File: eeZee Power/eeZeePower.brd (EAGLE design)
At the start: 26 x 12.7 mm, 11 parts

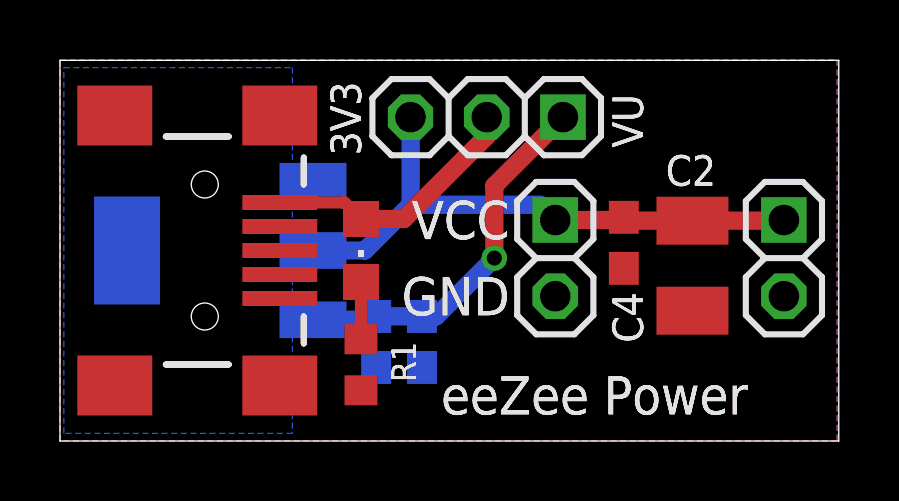
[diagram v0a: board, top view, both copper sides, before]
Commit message: Fixed jumper labels
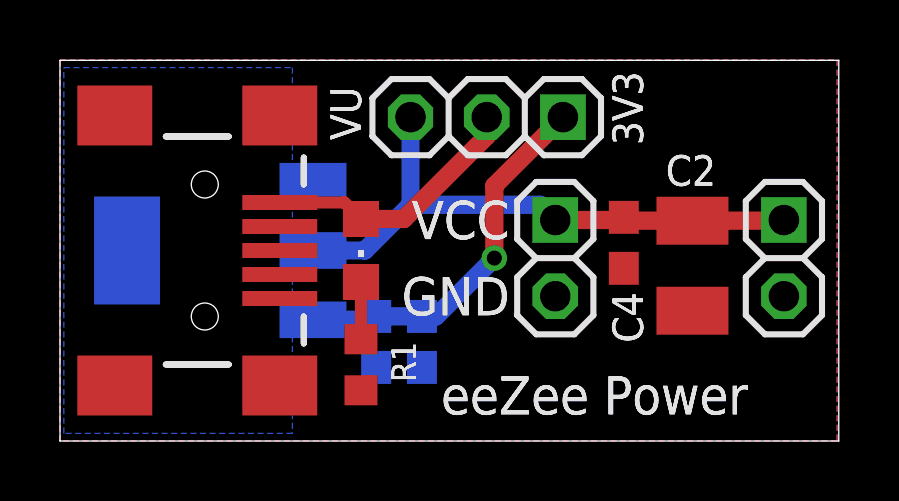
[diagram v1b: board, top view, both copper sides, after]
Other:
- board text added: "Rev 0.2"
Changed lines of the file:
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@@
 <layer number="19" name="Unrouted" color="6" fill="1" visible="yes" active="yes"/>
 <layer number="20" name="Dimension" color="15" fill="1" visible="yes" active="yes"/>
-<layer number="21" name="tPlace" color="7" fill="1" visible="no" active="yes"/>
+<layer number="21" name="tPlace" color="7" fill="1" visible="yes" active="yes"/>
 <layer number="22" name="bPlace" color="7" fill="1" visible="no" active="yes"/>
 <layer number="23" name="tOrigins" color="15" fill="1" visible="no" active="yes"/>
 <layer number="24" name="bOrigins" color="15" fill="1" visible="no" active="yes"/>
-<layer number="25" name="tNames" color="7" fill="1" visible="no" active="yes"/>
+<layer number="25" name="tNames" color="7" fill="1" visible="yes" active="yes"/>
 <layer number="26" name="bNames" color="7" fill="1" visible="no" active="yes"/>
 <layer number="27" name="tValues" color="7" fill="1" visible="no" active="yes"/>
@@
 <wire x1="25.959" y1="12.69" x2="0" y2="12.69" width="0" layer="20"/>
 <wire x1="0" y1="12.69" x2="0" y2="0" width="0" layer="20"/>
-<text x="18.415" y="11.557" size="1.016" layer="25" font="vector" rot="R270">VU</text>
+<text x="10.033" y="10.033" size="1.016" layer="25" font="vector" rot="R90">VU</text>
 <polygon width="0.254" layer="22">
 <vertex x="18.579675" y="10.0662625" curve="-9.499984"/>
@@
 <circle x="20.014540625" y="4.3887125" radius="0.115746875" width="0.231496875" layer="22"/>
 <circle x="21.548165625" y="3.81" radius="0.144678125" width="0.28935625" layer="22"/>
-<text x="10.033" y="9.525" size="1.016" layer="25" font="vector" rot="R90">3V3</text>
+<text x="18.415" y="12.319" size="1.016" layer="25" font="vector" rot="R270">3V3</text>
 <text x="12.7" y="0.889" size="1.27" layer="121" font="vector" ratio="16">eeZee Power</text>
 <wire x1="3.526003125" y1="10.14999375" x2="5.625996875" y2="10.14999375" width="0.2032" layer="121"/>
@@
 <rectangle x1="9.933" y1="6.15" x2="10.133" y2="6.35" layer="121" rot="R180"/>
 <text x="19.05" y="0.635" size="1.27" layer="122" font="vector" ratio="16" rot="MR0">bot-thoughts.com</text>
-<text x="1.27" y="11.811" size="1.27" layer="122" font="vector" ratio="16" rot="MR180">Rev 0.1</text>
+<text x="1.27" y="11.811" size="1.27" layer="122" font="vector" ratio="16" rot="MR180">Rev 0.2</text>
 <wire x1="18.365190625" y1="2.363190625" x2="18.365190625" y2="5.256809375" width="0.2032" layer="122"/>
 <wire x1="18.365190625" y1="5.256809375" x2="19.812" y2="5.256809375" width="0.2032" layer="122"/>
@@
 <vertex x="19.459678125" y="9.701759375"/>
 </polygon>
-<text x="18.415" y="11.557" size="1.016" layer="121" font="vector" ratio="20" rot="R270">VU</text>
+<text x="10.033" y="10.033" size="1.016" layer="121" font="vector" ratio="20" rot="R90">VU</text>
 <text x="14.986" y="8.001" size="1.27" layer="121" font="vector" ratio="16" rot="R180">VCC</text>
 <text x="14.986" y="5.461" size="1.27" layer="121" font="vector" ratio="16" rot="R180">GND</text>
-<text x="10.033" y="9.525" size="1.016" layer="121" font="vector" ratio="20" rot="R90">3V3</text>
+<text x="18.415" y="12.319" size="1.016" layer="121" font="vector" ratio="20" rot="R270">3V3</text>
 <text x="20.193" y="8.509" size="1.016" layer="121" font="vector" ratio="20">C2</text>
 <text x="18.415" y="4.953" size="1.016" layer="121" font="vector" ratio="20" rot="R270">C4</text>
